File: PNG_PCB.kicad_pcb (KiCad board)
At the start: 2 copper layers, 109 parts, among them J1 screw term, J10 screw term, J11 screw term, J12 screw term, J13 screw term, J14 screw term, J15 screw term, J16 screw term, J17 screw term, J18 screw term, J19 screw term, J2 screw term, J20 screw term, J21 screw term, J22 screw term, J23 screw term, J24 screw term, J25 screw term, J26 screw term, J27 screw term, J28 screw term, J29 screw term, J3 screw term, J30 screw term, J4 screw term, J5 screw term, J6 screw term, J7 screw term, J8 screw term, J9 screw term, U1 Teensy4.1, U2 Mux, U3 MCP6004, U4 Mux, U5 Mux, U6 MCP6004, U7 Mux, U8 Mux, U9 MCP6004

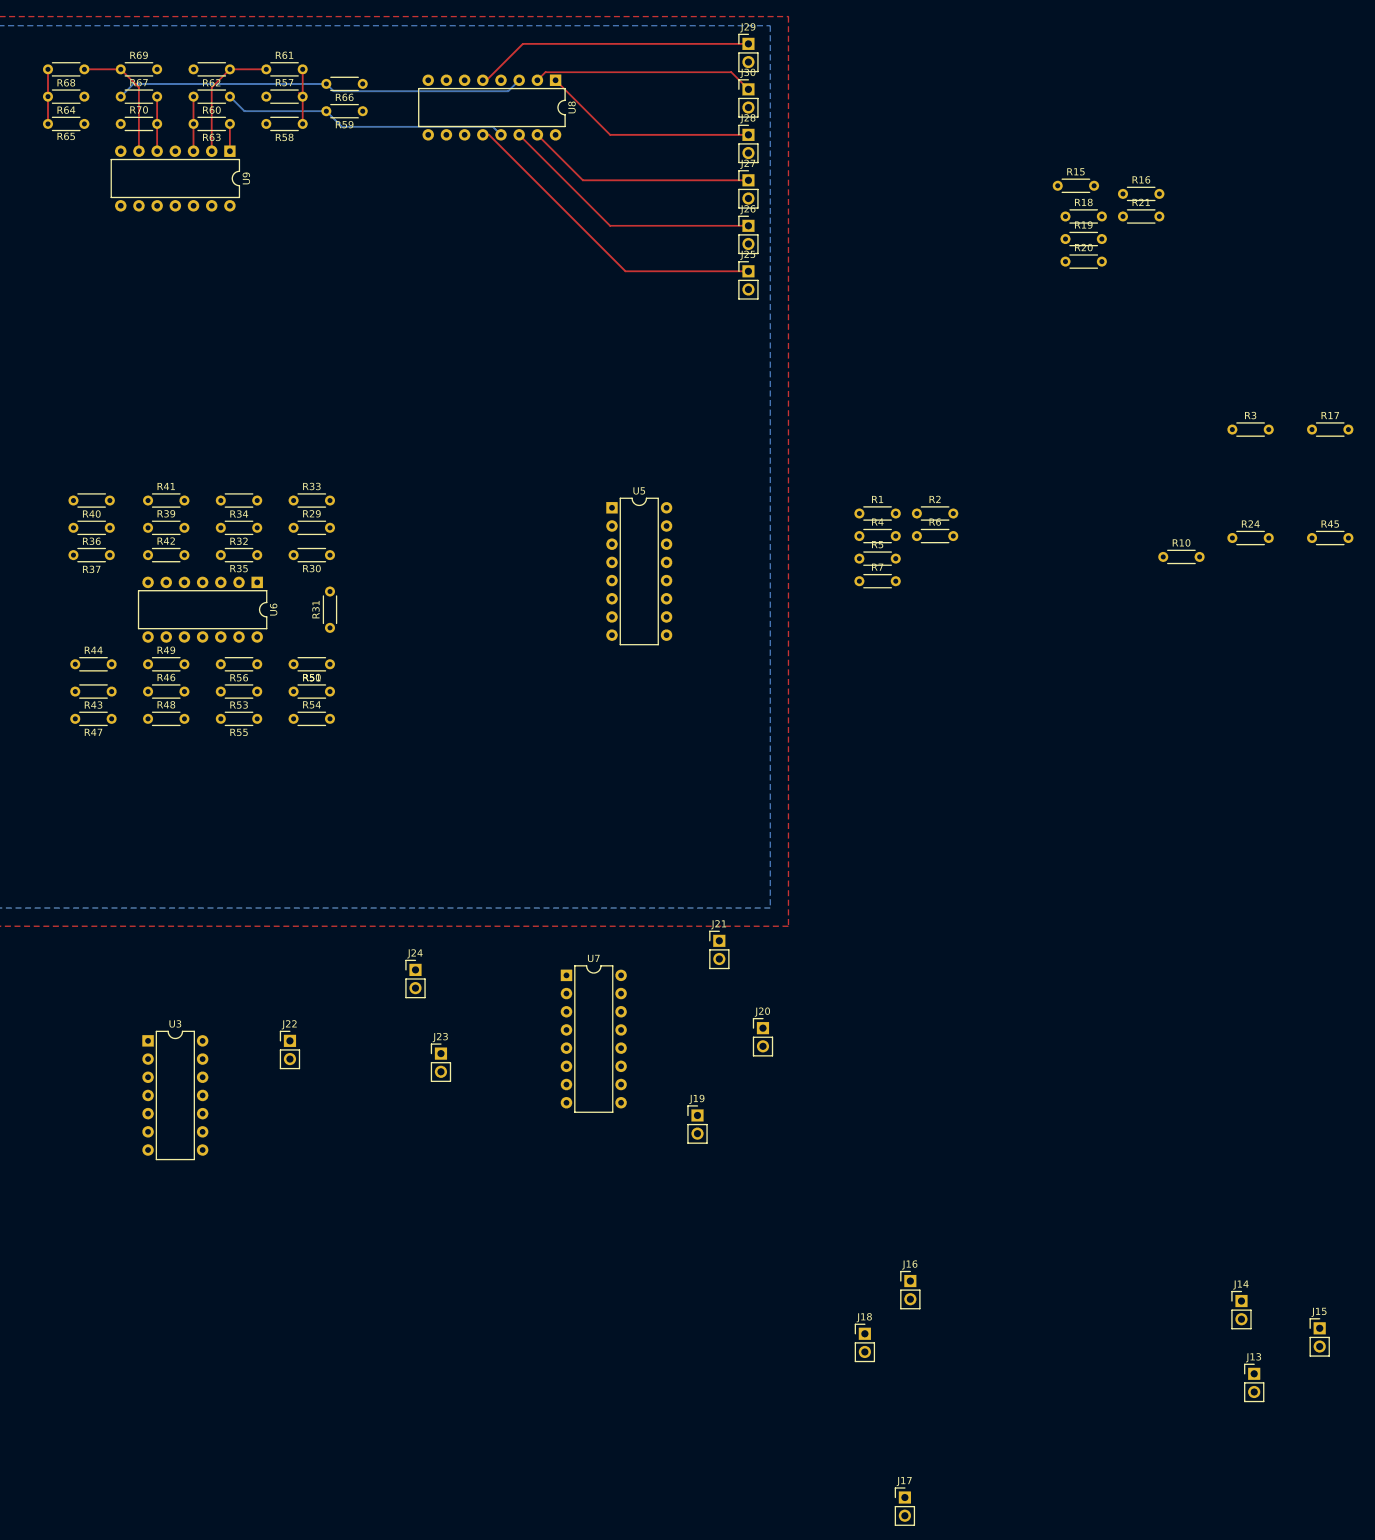
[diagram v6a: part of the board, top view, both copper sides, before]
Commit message: top mux connected to final position
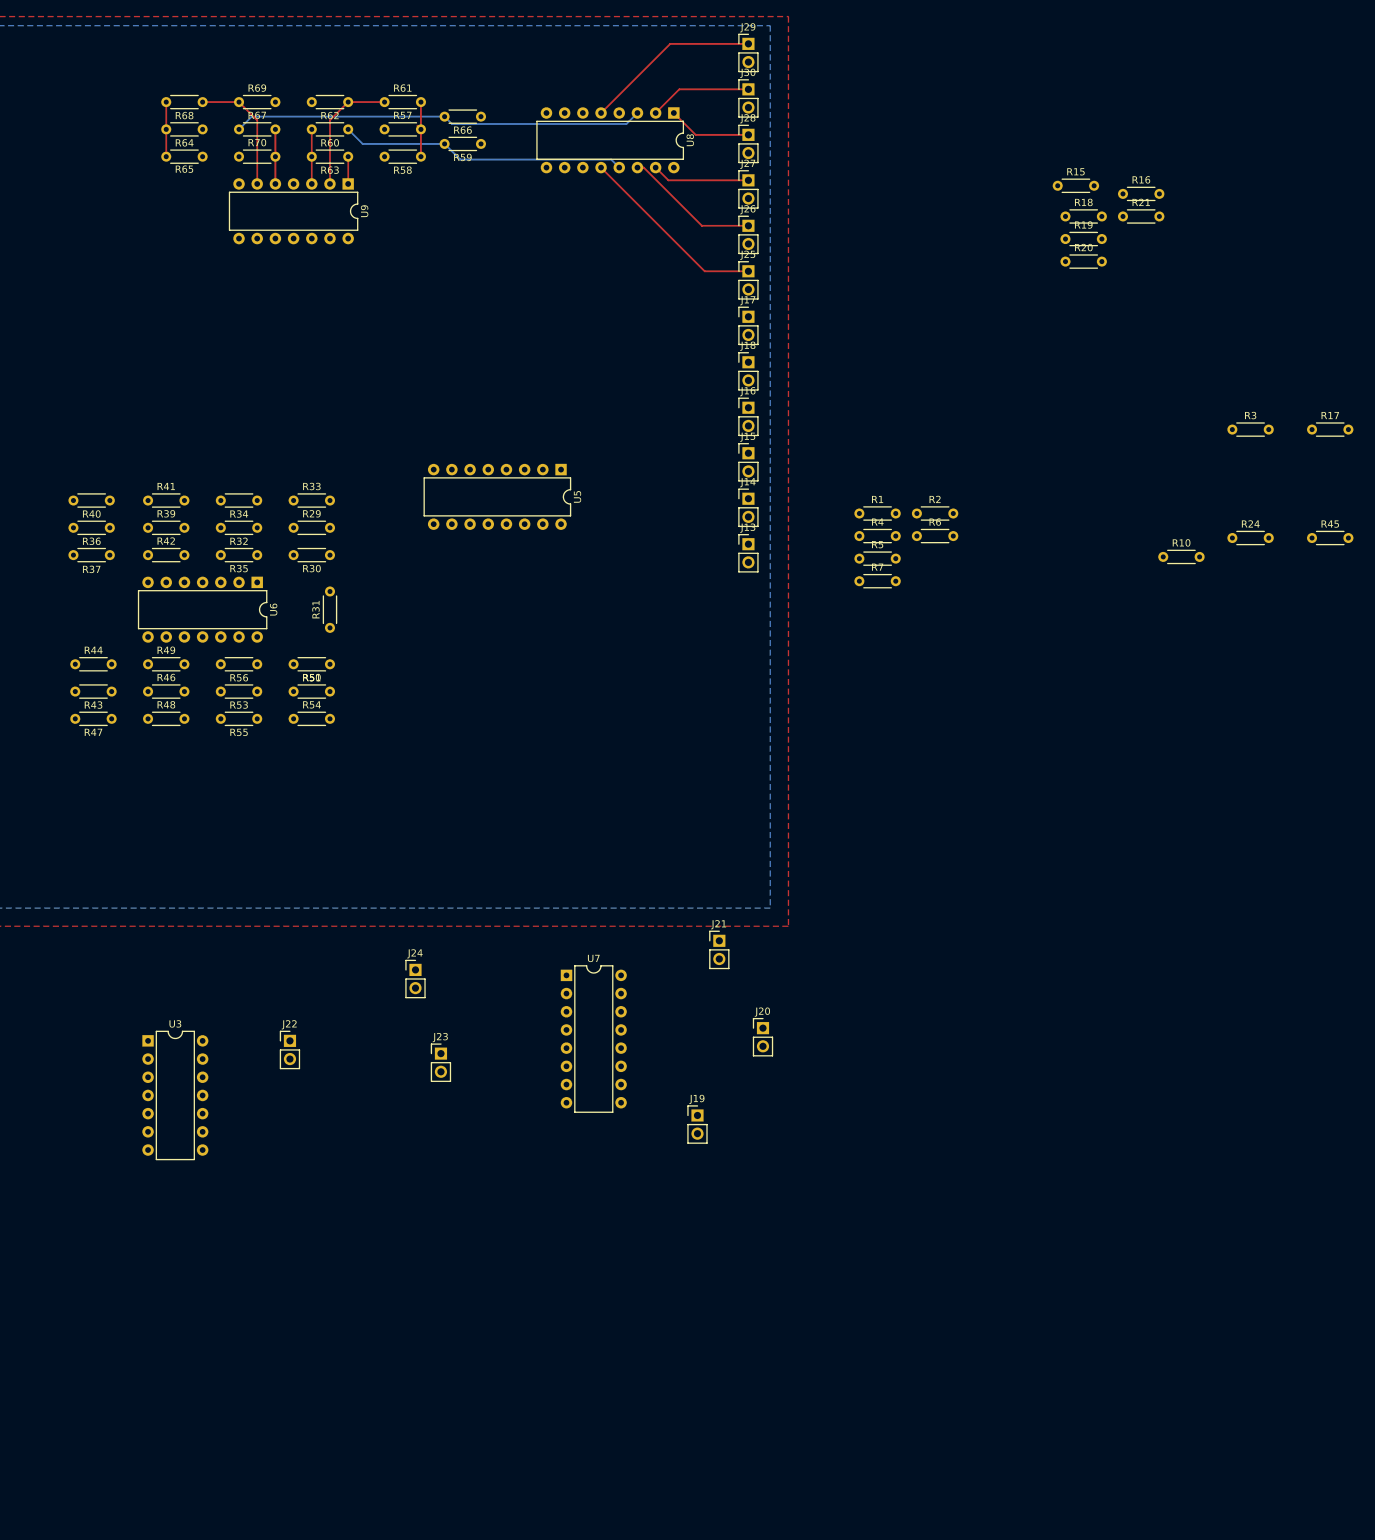
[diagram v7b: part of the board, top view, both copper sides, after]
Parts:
- moved J17 166.3 mm to (252.2, 92.7)
- moved J15 145.9 mm to (252.2, 111.8)
- moved J18 136.6 mm to (252.2, 99.1)
- moved J13 135.7 mm to (252.2, 124.5)
- moved J14 131.5 mm to (252.2, 118.1)
- moved J16 124.0 mm to (252.2, 105.4)
- moved R58 17.1 mm to (206.5, 70.4)
- moved R60 17.1 mm to (196.3, 66.5)
- moved R62 17.1 mm to (196.3, 62.7)
- moved R63 17.1 mm to (196.3, 70.4)
- moved R65 17.1 mm to (170.9, 70.4)
- moved U9 17.1 mm to (196.3, 74.2)
- moved R57 17.1 mm to (201.4, 66.5)
- moved R59 17.1 mm to (214.9, 68.6)
- moved R61 17.1 mm to (201.4, 62.7)
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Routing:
- net /ampA2/mux1: track 37.3 -> 18.9 mm
- net /ampA2/mux0: track 45.0 -> 26.6 mm
- net /ampA2/mux2: track 32.1 -> 13.7 mm
- net /ampB2/mux0: track 30.1 -> 11.7 mm
- net /ampB2/mux2: track 30.9 -> 14.3 mm
- net /ampB2/mux1: track 39.2 -> 24.6 mm

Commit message: wired up the middle amp
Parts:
- moved R11 283.4 mm to (165.8, 228.1)
- moved R12 283.4 mm to (173.8, 221.8)
- moved R13 283.4 mm to (165.8, 224.9)
- moved R14 283.4 mm to (165.8, 221.8)
- moved R22 283.4 mm to (144.7, 234.9)
- moved R23 283.4 mm to (152.8, 241.2)
- moved R25 283.4 mm to (152.8, 238.1)
- moved R26 283.4 mm to (144.7, 241.2)
- moved R27 283.4 mm to (152.8, 234.9)
- moved R28 283.4 mm to (144.7, 238.1)
- moved R8 283.4 mm to (173.8, 228.1)
- moved R9 283.4 mm to (173.8, 224.9)
- moved R10 144.6 mm to (191.8, 209.3)
- moved R17 144.6 mm to (212.5, 191.5)
- moved R24 144.6 mm to (201.4, 206.7)
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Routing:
- net /ampC1/V1: track 0.00 -> 29.5 mm
- net /ampB1/V1: track 0.00 -> 29.2 mm
- net /ampB1/mux1: track 0.00 -> 25.8 mm
- net /ampD1/mux1: track 0.00 -> 25.6 mm
- net /ampA1/mux0: track 0.00 -> 25.3 mm
- net /ampC1/mux0: track 0.00 -> 25.1 mm
- net Net-(R40-Pad1): track 0.00 -> 17.8 mm
- net /ampA1/mux1: track 0.00 -> 17.6 mm
- net Net-(R54-Pad1): track 0.00 -> 17.6 mm
- net Net-(R47-Pad1): track 0.00 -> 17.6 mm
- net Net-(R33-Pad1): track 0.00 -> 17.6 mm
- net /ampC1/mux1: track 0.00 -> 17.3 mm
- net /ampB1/mux2: track 0.00 -> 15.6 mm
- net /ampD1/mux2: track 0.00 -> 15.3 mm
- net /ampD1/V1: track 0.00 -> 14.2 mm
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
